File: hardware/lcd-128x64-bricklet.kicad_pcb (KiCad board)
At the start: 2 copper layers, 95 x 55 mm, 44 parts, among them P1 CON-SENSOR2, P2 Debug, P3 BOOT, P4 CON_4Wire_ER-TP028-1, Q1 2N7002, U1 XMC130024, U2 TSC2046E, U3 LCD-ERC12864, U4 DRILL, U5 DRILL, U6 DRILL, U7 DRILL

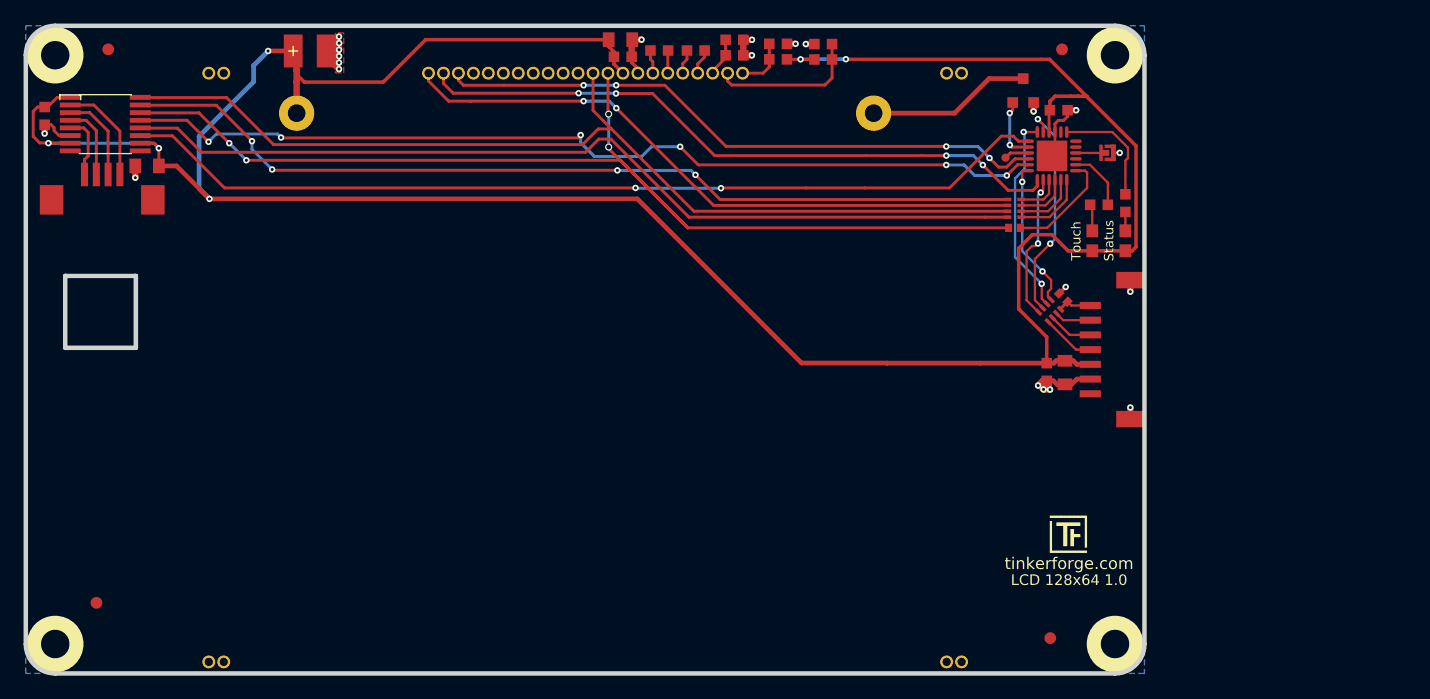
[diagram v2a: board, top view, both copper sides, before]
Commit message: change lcd128 footprint
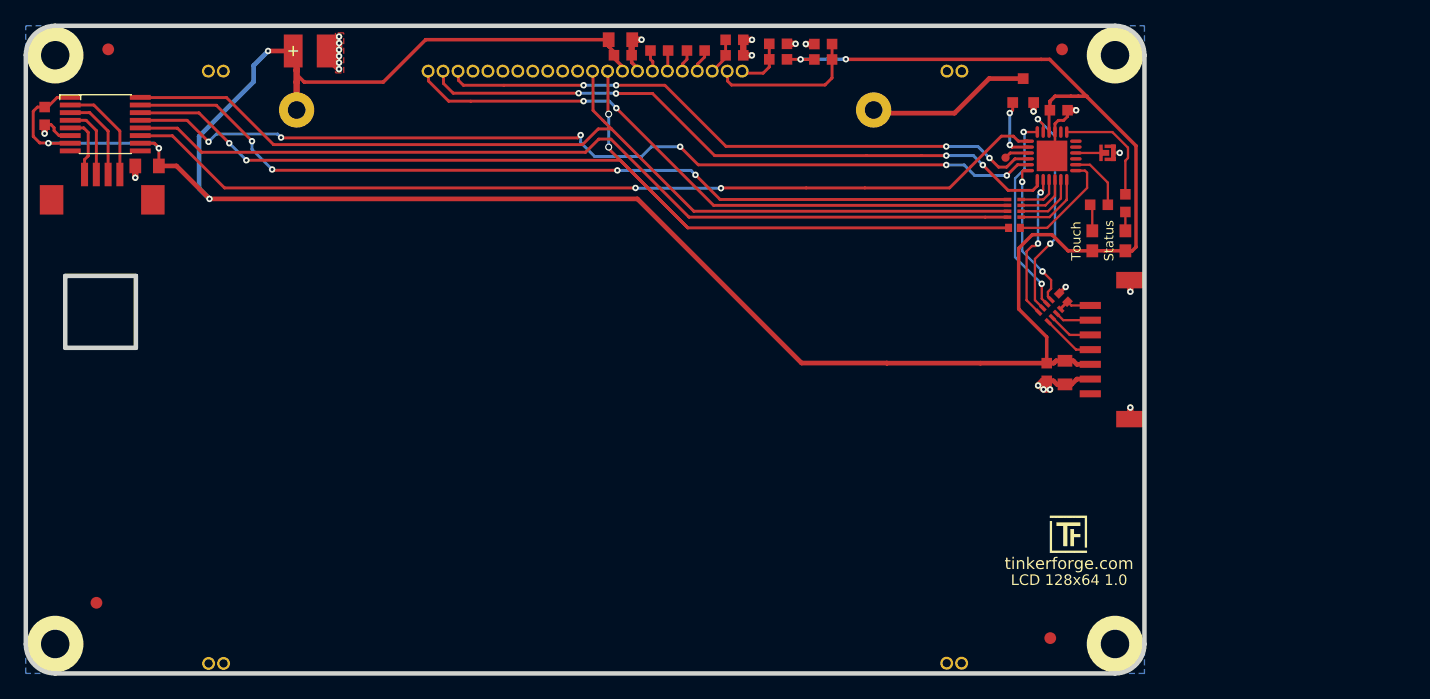
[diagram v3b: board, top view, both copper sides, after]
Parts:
- moved C11 0.13 mm to (142.6, 63.8)
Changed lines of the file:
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@@
     (links 100)
     (no_connects 0)
-    (area 91.709499 61.109499 187.090501 116.490501)
+    (area 91.044999 60.444999 187.755001 117.155001)
     (thickness 1.6)
     (drawings 16)
@@
   )
   (setup
-    (last_trace_width 0.25)
+    (last_trace_width 0.3)
     (user_trace_width 0.2)
     (user_trace_width 0.25)
@@
   )
   (module kicad-libraries:C0603F (layer F.Cu)
-    (at 142.6 63.93 180)
+    (at 142.6 63.8 180)
     (attr smd)
     (fp_text reference C11 (at 0.05 0.225 180) (layer F.Fab)
@@
   )
   (module kicad-libraries:ERC12864-655_128x64 (layer F.Cu)
-    (at 139.4 90.32)
+    (at 139.4 90.3)
     (fp_text reference U3 (at 0 -1.82) (layer F.Fab)
       (effects (font (size 1 1) (thickness 0.15)))
@@
     (fp_line (start 35 25) (end 35 -25) (layer F.Fab) (width 0.2))
     (fp_line (start 35 -25) (end -35 -25) (layer F.Fab) (width 0.2))
-    (pad NC thru_hole circle (at -31.96 25) (size 1.1 1.1) (drill 0.7) (layers *.Cu *.Mask F.SilkS))
-    (pad NC thru_hole circle (at 31.97 25) (size 1.1 1.1) (drill 0.7) (layers *.Cu *.Mask F.SilkS))
-    (pad NC thru_hole circle (at 30.7 25) (size 1.1 1.1) (drill 0.7) (layers *.Cu *.Mask F.SilkS))
-    (pad NC thru_hole circle (at -30.69 25) (size 1.1 1.1) (drill 0.7) (layers *.Cu *.Mask F.SilkS))
-    (pad NC thru_hole circle (at -31.96 -25) (size 1.1 1.1) (drill 0.7) (layers *.Cu *.Mask F.SilkS))
-    (pad NC thru_hole circle (at -30.69 -25) (size 1.1 1.1) (drill 0.7) (layers *.Cu *.Mask F.SilkS))
-    (pad NC thru_hole circle (at 31.97 -25) (size 1.1 1.1) (drill 0.7) (layers *.Cu *.Mask F.SilkS))
-    (pad NC thru_hole circle (at 30.7 -25) (size 1.1 1.1) (drill 0.7) (layers *.Cu *.Mask F.SilkS))
-    (pad 1 thru_hole circle (at -13.3 -25) (size 1.1 1.1) (drill 0.7) (layers *.Cu *.Mask F.SilkS)
+    (pad NC thru_hole circle (at -31.975 25.15) (size 1.1 1.1) (drill 0.7) (layers *.Cu *.Mask F.SilkS))
+    (pad NC thru_hole circle (at 31.975 25.13) (size 1.1 1.1) (drill 0.7) (layers *.Cu *.Mask F.SilkS))
+    (pad NC thru_hole circle (at 30.705 25.13) (size 1.1 1.1) (drill 0.7) (layers *.Cu *.Mask F.SilkS))
+    (pad NC thru_hole circle (at -30.705 25.15) (size 1.1 1.1) (drill 0.7) (layers *.Cu *.Mask F.SilkS))
+    (pad NC thru_hole circle (at -31.995 -25.15) (size 1.1 1.1) (drill 0.7) (layers *.Cu *.Mask F.SilkS))
+    (pad NC thru_hole circle (at -30.725 -25.15) (size 1.1 1.1) (drill 0.7) (layers *.Cu *.Mask F.SilkS))
+    (pad NC thru_hole circle (at 31.995 -25.15) (size 1.1 1.1) (drill 0.7) (layers *.Cu *.Mask F.SilkS))
+    (pad NC thru_hole circle (at 30.725 -25.15) (size 1.1 1.1) (drill 0.7) (layers *.Cu *.Mask F.SilkS))
+    (pad 1 thru_hole circle (at -13.335 -25.15) (size 1.1 1.1) (drill 0.7) (layers *.Cu *.Mask F.SilkS)
       (net 31 M-CS-LCD))
-    (pad 2 thru_hole circle (at -12.03 -25) (size 1.1 1.1) (drill 0.7) (layers *.Cu *.Mask F.SilkS)
+    (pad 2 thru_hole circle (at -12.065 -25.15) (size 1.1 1.1) (drill 0.7) (layers *.Cu *.Mask F.SilkS)
       (net 37 LCD-RST))
-    (pad 3 thru_hole circle (at -10.76 -25) (size 1.1 1.1) (drill 0.7) (layers *.Cu *.Mask F.SilkS)
+    (pad 3 thru_hole circle (at -10.795 -25.15) (size 1.1 1.1) (drill 0.7) (layers *.Cu *.Mask F.SilkS)
       (net 40 LCD-CD))
-    (pad 4 thru_hole circle (at -9.49 -25) (size 1.1 1.1) (drill 0.7) (layers *.Cu *.Mask F.SilkS)
+    (pad 4 thru_hole circle (at -9.525 -25.15) (size 1.1 1.1) (drill 0.7) (layers *.Cu *.Mask F.SilkS)
       (net 1 GND))
-    (pad 5 thru_hole circle (at -8.22 -25) (size 1.1 1.1) (drill 0.7) (layers *.Cu *.Mask F.SilkS)
+    (pad 5 thru_hole circle (at -8.255 -25.15) (size 1.1 1.1) (drill 0.7) (layers *.Cu *.Mask F.SilkS)
       (net 1 GND))
-    (pad 6 thru_hole circle (at -6.95 -25) (size 1.1 1.1) (drill 0.7) (layers *.Cu *.Mask F.SilkS)
+    (pad 6 thru_hole circle (at -6.985 -25.15) (size 1.1 1.1) (drill 0.7) (layers *.Cu *.Mask F.SilkS)
       (net 1 GND))
-    (pad 7 thru_hole circle (at -5.68 -25) (size 1.1 1.1) (drill 0.7) (layers *.Cu *.Mask F.SilkS)
+    (pad 7 thru_hole circle (at -5.715 -25.15) (size 1.1 1.1) (drill 0.7) (layers *.Cu *.Mask F.SilkS)
       (net 1 GND))
-    (pad 8 thru_hole circle (at -4.41 -25) (size 1.1 1.1) (drill 0.7) (layers *.Cu *.Mask F.SilkS)
+    (pad 8 thru_hole circle (at -4.445 -25.15) (size 1.1 1.1) (drill 0.7) (layers *.Cu *.Mask F.SilkS)
       (net 1 GND))
-    (pad 9 thru_hole circle (at -3.14 -25) (size 1.1 1.1) (drill 0.7) (layers *.Cu *.Mask F.SilkS)
+    (pad 9 thru_hole circle (at -3.175 -25.15) (size 1.1 1.1) (drill 0.7) (layers *.Cu *.Mask F.SilkS)
       (net 1 GND))
-    (pad 10 thru_hole circle (at -1.87 -25) (size 1.1 1.1) (drill 0.7) (layers *.Cu *.Mask F.SilkS)
+    (pad 10 thru_hole circle (at -1.905 -25.15) (size 1.1 1.1) (drill 0.7) (layers *.Cu *.Mask F.SilkS)
       (net 1 GND))
-    (pad 11 thru_hole circle (at -0.6 -25) (size 1.1 1.1) (drill 0.7) (layers *.Cu *.Mask F.SilkS)
+    (pad 11 thru_hole circle (at -0.635 -25.15) (size 1.1 1.1) (drill 0.7) (layers *.Cu *.Mask F.SilkS)
       (net 1 GND))
-    (pad 12 thru_hole circle (at 0.67 -25) (size 1.1 1.1) (drill 0.7) (layers *.Cu *.Mask F.SilkS)
+    (pad 12 thru_hole circle (at 0.635 -25.15) (size 1.1 1.1) (drill 0.7) (layers *.Cu *.Mask F.SilkS)
       (net 32 M-CLK))
-    (pad 13 thru_hole circle (at 1.94 -25) (size 1.1 1.1) (drill 0.7) (layers *.Cu *.Mask F.SilkS)
+    (pad 13 thru_hole circle (at 1.905 -25.15) (size 1.1 1.1) (drill 0.7) (layers *.Cu *.Mask F.SilkS)
       (net 41 M-MOSI))
-    (pad 14 thru_hole circle (at 3.21 -25) (size 1.1 1.1) (drill 0.7) (layers *.Cu *.Mask F.SilkS)
+    (pad 14 thru_hole circle (at 3.175 -25.15) (size 1.1 1.1) (drill 0.7) (layers *.Cu *.Mask F.SilkS)
       (net 3 VCC))
-    (pad 15 thru_hole circle (at 4.48 -25) (size 1.1 1.1) (drill 0.7) (layers *.Cu *.Mask F.SilkS)
+    (pad 15 thru_hole circle (at 4.445 -25.15) (size 1.1 1.1) (drill 0.7) (layers *.Cu *.Mask F.SilkS)
       (net 1 GND))
-    (pad 16 thru_hole circle (at 5.75 -25) (size 1.1 1.1) (drill 0.7) (layers *.Cu *.Mask F.SilkS)
+    (pad 16 thru_hole circle (at 5.715 -25.15) (size 1.1 1.1) (drill 0.7) (layers *.Cu *.Mask F.SilkS)
       (net 8 "Net-(C10-Pad2)"))
-    (pad 17 thru_hole circle (at 7.02 -25) (size 1.1 1.1) (drill 0.7) (layers *.Cu *.Mask F.SilkS)
+    (pad 17 thru_hole circle (at 6.985 -25.15) (size 1.1 1.1) (drill 0.7) (layers *.Cu *.Mask F.SilkS)
       (net 7 "Net-(C10-Pad1)"))
-    (pad 18 thru_hole circle (at 8.29 -25) (size 1.1 1.1) (drill 0.7) (layers *.Cu *.Mask F.SilkS)
+    (pad 18 thru_hole circle (at 8.255 -25.15) (size 1.1 1.1) (drill 0.7) (layers *.Cu *.Mask F.SilkS)
       (net 5 "Net-(C9-Pad1)"))
-    (pad 19 thru_hole circle (at 9.56 -25) (size 1.1 1.1) (drill 0.7) (layers *.Cu *.Mask F.SilkS)
+    (pad 19 thru_hole circle (at 9.525 -25.15) (size 1.1 1.1) (drill 0.7) (layers *.Cu *.Mask F.SilkS)
       (net 6 "Net-(C9-Pad2)"))
-    (pad 20 thru_hole circle (at 10.83 -25) (size 1.1 1.1) (drill 0.7) (layers *.Cu *.Mask F.SilkS)
+    (pad 20 thru_hole circle (at 10.795 -25.15) (size 1.1 1.1) (drill 0.7) (layers *.Cu *.Mask F.SilkS)
       (net 4 "Net-(C7-Pad1)"))
-    (pad 21 thru_hole circle (at 12.1 -25) (size 1.1 1.1) (drill 0.7) (layers *.Cu *.Mask F.SilkS)
+    (pad 21 thru_hole circle (at 12.065 -25.15) (size 1.1 1.1) (drill 0.7) (layers *.Cu *.Mask F.SilkS)
       (net 23 "Net-(R4-Pad2)"))
-    (pad 22 thru_hole circle (at 13.37 -25) (size 1.1 1.1) (drill 0.7) (layers *.Cu *.Mask F.SilkS)
+    (pad 22 thru_hole circle (at 13.335 -25.15) (size 1.1 1.1) (drill 0.7) (layers *.Cu *.Mask F.SilkS)
       (net 22 "Net-(R2-Pad2)"))
-    (pad 23 thru_hole circle (at -24.5 -21.6) (size 3 3) (drill 1.5) (layers *.Cu *.Mask F.SilkS)
+    (pad 23 thru_hole circle (at -24.5 -21.85) (size 3 3) (drill 1.5) (layers *.Cu *.Mask F.SilkS)
       (net 3 VCC))
-    (pad 24 thru_hole circle (at 24.5 -21.6) (size 3 3) (drill 1.5) (layers *.Cu *.Mask F.SilkS)
+    (pad 24 thru_hole circle (at 24.5 -21.85) (size 3 3) (drill 1.5) (layers *.Cu *.Mask F.SilkS)
       (net 20 "Net-(Q1-PadD)"))
   )
@@
   (segment (start 182.3 84.99) (end 182.3 85.05) (width 0.25) (layer F.Cu) (net 2))
   (segment (start 182.3 85.05) (end 182.3 84.89) (width 0.25) (layer F.Cu) (net 2))
+  (segment (start 142.575 65.15) (end 142.575 64.775) (width 0.3) (layer F.Cu) (net 3))
+  (segment (start 142.575 64.775) (end 141.85 64.05) (width 0.3) (layer F.Cu) (net 3))
+  (segment (start 141.85 64.05) (end 141.85 63.8) (width 0.3) (layer F.Cu) (net 3))
   (segment (start 107.495 75.995) (end 107.5 76) (width 0.4) (layer F.Cu) (net 3))
   (via (at 107.5 76) (size 0.55) (drill 0.25) (layers F.Cu B.Cu) (net 3))
@@
   (segment (start 157.7 64.15) (end 158.86 64.15) (width 0.25) (layer F.Cu) (net 3))
   (segment (start 158.86 64.15) (end 158.87 64.16) (width 0.25) (layer F.Cu) (net 3))
-  (segment (start 141.85 64.56) (end 142.61 65.32) (width 0.3) (layer F.Cu) (net 3))
-  (segment (start 141.85 63.93) (end 141.85 64.56) (width 0.3) (layer F.Cu) (net 3))
   (segment (start 141.85 63.93) (end 141.85 63.51) (width 0.3) (layer F.Cu) (net 3))
   (segment (start 141.85 63.51) (end 141.39924 63.05924) (width 0.3) (layer F.Cu) (net 3))
@@
   (segment (start 114.9 63.60048) (end 114.59952 63.3) (width 0.55) (layer F.Cu) (net 3))
   (segment (start 141.39924 62.3) (end 141.39924 62.69924) (width 0.25) (layer F.Cu) (net 3))
-  (segment (start 141.85 64.15) (end 141.85 63.8) (width 0.25) (layer F.Cu) (net 3))
   (segment (start 151.33 63.81) (end 151.33 62.49) (width 0.25) (layer F.Cu) (net 4))
   (segment (start 150.23 65.32) (end 150.23 65.13) (width 0.25) (layer F.Cu) (net 4))

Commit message: Add new layout (tbc)
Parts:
- added R9: 27|22, R1206, F.Cu at (156.7, 72.4)
- U3: moved to B.Cu
- moved Fiducial_Mark 95.1 mm to (185.1, 72.2)
- moved Fiducial_Mark 89.4 mm to (187.7, 74.3)
- moved C6 75.1 mm to (159.7, 104.4)
- moved U2 75.0 mm to (164.6, 105.4)
- moved C5 72.1 mm to (164.8, 108.9)
- moved P4 71.7 mm to (164.7, 101.2), turned to 180 degrees
- moved VAL 67.5 mm to (191.8, 67.9)
- moved Q1 61.0 mm to (116.2, 75.2), turned to 270 degrees
- moved G*** 50.8 mm to (185.3, 67.0)
- moved VAL 44.6 mm to (192.1, 74.1)
- moved G*** 42.8 mm to (200.6, 66.0)
- moved Fiducial_Mark 41.9 mm to (187.9, 72.4)
- moved C8 41.3 mm to (155.3, 76.3), turned to 270 degrees
- moved R5 35.9 mm to (124.7, 71.4)
- moved R4 35.4 mm to (124.7, 70.0)
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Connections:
- C8 pad 1: VCC -> +5V
- P1 pad 1: (no net) -> +5V
- U1 pad 3: (no net) -> Net-(U1-Pad3)
- U1 pad 5: (no net) -> Net-(U1-Pad5)
- U1 pad 6: (no net) -> Net-(U1-Pad6)
- U1 pad 8: (no net) -> Net-(U1-Pad8)
- U2 pad 8: (no net) -> Net-(U2-Pad8)
- U2 pad 9: (no net) -> Net-(U2-Pad9)
- U3 pad 23: VCC -> Net-(R9-Pad1)
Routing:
- net VCC: track 233.8 -> 35.8 mm, vias 6 -> 0
- net PENIRQ: track 79.5 -> 0.00 mm, vias 2 -> 0
- net TS-BUSY: track 79.5 -> 0.00 mm, vias 6 -> 0
- net M-MISO: track 77.3 -> 0.00 mm
- net M-CS-TS: track 77.2 -> 0.00 mm, vias 4 -> 0
- net LCD-RST: track 55.7 -> 0.00 mm, vias 4 -> 0
- net M-MOSI: track 93.4 -> 39.8 mm, vias 4 -> 0
- net SW-BACK: track 5.60 -> 59.1 mm, vias 2 -> 4
- net LCD-CD: track 52.5 -> 0.00 mm, vias 4 -> 0
- net M-CLK: track 84.2 -> 39.8 mm
- net +5V: track 0.00 -> 38.5 mm
- net M-CS-LCD: track 54.2 -> 25.3 mm, vias 2 -> 0
- net GND: track 45.1 -> 55.6 mm, vias 22 -> 25
- net Net-(R9-Pad1): track 0.00 -> 10.3 mm
- net Net-(R1-Pad1): track 9.80 -> 0.00 mm
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- removed copper zone on F.Cu, net GND
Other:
- board size 95 x 55 mm -> 85 x 55 mm

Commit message: Add new layout
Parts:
- G***: moved to B.Cu
- G***, VAL (x2): moved to F.Cu
- moved G*** 102.8 mm to (102.4, 96.7), turned to 180 degrees
- moved Fiducial_Mark 92.0 mm to (102.4, 108.8)
- moved Fiducial_Mark 88.5 mm to (99.4, 73.8)
- moved VAL 67.3 mm to (126.4, 88.8), turned to 0 degrees
- moved G*** 50.8 mm to (139.4, 88.8), turned to 0 degrees
- moved VAL 44.6 mm to (152.4, 88.8), turned to 0 degrees
- moved Fiducial_Mark 37.6 mm to (176.4, 110.8)
- moved P3 18.3 mm to (166.4, 72.2)
- moved P2 12.6 mm to (172.3, 84.2)
- moved Fiducial_Mark 7.49 mm to (178.4, 68.8)
- moved RP2 3.02 mm to (177.2, 74.7), turned to 180 degrees
- moved C11 1.67 mm to (135.8, 70.0)
- moved C12 1.38 mm to (136.0, 71.5)
- moved R7 0.38 mm to (173.3, 73.4)
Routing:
- net VCC: track 35.8 -> 171.3 mm, vias 0 -> 2
- net M-CLK: track 39.8 -> 82.2 mm, vias 0 -> 2
- net M-MOSI: track 39.8 -> 81.0 mm, vias 0 -> 2
- net M-CS-TS: track 0.00 -> 40.9 mm, vias 0 -> 2
- net M-MISO: track 0.00 -> 40.7 mm, vias 0 -> 2
- net LCD-CD: track 0.00 -> 40.7 mm, vias 0 -> 2
- net PENIRQ: track 0.00 -> 39.0 mm, vias 0 -> 2
- net LCD-RST: track 0.00 -> 38.1 mm, vias 0 -> 2
- net TS-BUSY: track 0.00 -> 32.8 mm, vias 0 -> 2
- net Net-(R1-Pad1): track 0.00 -> 15.3 mm, vias 0 -> 2
- net Net-(D2-Pad2): track 0.00 -> 6.10 mm
- net Net-(D1-Pad2): track 0.00 -> 6.10 mm
- net Net-(P2-Pad1): track 0.00 -> 5.12 mm
- net GND: track 55.6 -> 60.6 mm
- net Net-(RP2-Pad8): track 8.71 -> 4.28 mm
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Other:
- board text added: "1.0"
- board text added: "LCD 128x64"
- board text removed: "LCD 128x64 1.0"
